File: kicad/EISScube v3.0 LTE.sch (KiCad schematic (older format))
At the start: 0 parts

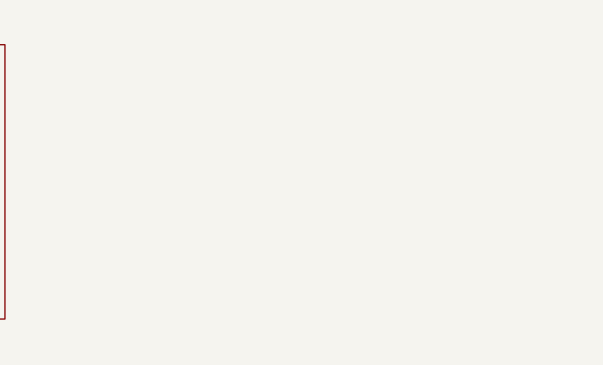
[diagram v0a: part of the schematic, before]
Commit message: add visual references are called “fiducials“ on board for PnP machine
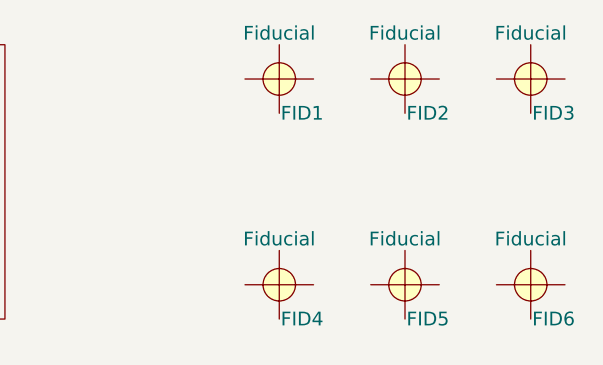
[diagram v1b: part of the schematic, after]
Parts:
- added FID1, FID2, FID3: Fiducial, Fiducials:Fiducial_1mm_Dia_2.54mm_Outer_CopperTop, symbol Fiducial
- added FID4, FID5, FID6: Fiducial, Fiducials:Fiducial_1mm_Dia_2.54mm_Outer_CopperBottom, symbol Fiducial
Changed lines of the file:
@@
 F1 "EISScube-pw.sch" 60
 $EndSheet
+$Comp
+L Fiducial FID1
+U 1 1 5AE0BAFC
+P 6100 1100
+F 0 "FID1" H 6200 950 60  0000 C CNN
+F 1 "Fiducial" H 6100 1300 60  0000 C CNN
+F 2 "Fiducials:Fiducial_1mm_Dia_2.54mm_Outer_CopperTop" H 6100 1100 60  0001 C CNN
+F 3 "" H 6100 1100 60  0001 C CNN
+	1    6100 1100
+	1    0    0    -1
+$EndComp
+$Comp
+L Fiducial FID2
+U 1 1 5AE0BB64
+P 6650 1100
+F 0 "FID2" H 6750 950 60  0000 C CNN
+F 1 "Fiducial" H 6650 1300 60  0000 C CNN
+F 2 "Fiducials:Fiducial_1mm_Dia_2.54mm_Outer_CopperTop" H 6650 1100 60  0001 C CNN
+F 3 "" H 6650 1100 60  0001 C CNN
+	1    6650 1100
+	1    0    0    -1
+$EndComp
+$Comp
+L Fiducial FID3
+U 1 1 5AE0BBCA
+P 7200 1100
+F 0 "FID3" H 7300 950 60  0000 C CNN
+F 1 "Fiducial" H 7200 1300 60  0000 C CNN
+F 2 "Fiducials:Fiducial_1mm_Dia_2.54mm_Outer_CopperTop" H 7200 1100 60  0001 C CNN
+F 3 "" H 7200 1100 60  0001 C CNN
+	1    7200 1100
+	1    0    0    -1
+$EndComp
+$Comp
+L Fiducial FID4
+U 1 1 5AE0BCF1
+P 6100 2000
+F 0 "FID4" H 6200 1850 60  0000 C CNN
+F 1 "Fiducial" H 6100 2200 60  0000 C CNN
+F 2 "Fiducials:Fiducial_1mm_Dia_2.54mm_Outer_CopperBottom" H 6100 2000 60  0001 C CNN
+F 3 "" H 6100 2000 60  0001 C CNN
+	1    6100 2000
+	1    0    0    -1
+$EndComp
+$Comp
+L Fiducial FID5
+U 1 1 5AE0BD24
+P 6650 2000
+F 0 "FID5" H 6750 1850 60  0000 C CNN
+F 1 "Fiducial" H 6650 2200 60  0000 C CNN
+F 2 "Fiducials:Fiducial_1mm_Dia_2.54mm_Outer_CopperBottom" H 6650 2000 60  0001 C CNN
+F 3 "" H 6650 2000 60  0001 C CNN
+	1    6650 2000
+	1    0    0    -1
+$EndComp
+$Comp
+L Fiducial FID6
+U 1 1 5AE0BD54
+P 7200 2000
+F 0 "FID6" H 7300 1850 60  0000 C CNN
+F 1 "Fiducial" H 7200 2200 60  0000 C CNN
+F 2 "Fiducials:Fiducial_1mm_Dia_2.54mm_Outer_CopperBottom" H 7200 2000 60  0001 C CNN
+F 3 "" H 7200 2000 60  0001 C CNN
+	1    7200 2000
+	1    0    0    -1
+$EndComp
 $EndSCHEMATC
